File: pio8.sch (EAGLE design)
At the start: 35 parts, among them IC1 DS2408, X1 MSTBV3, X7 MSTBV5, X8 MSTBV5

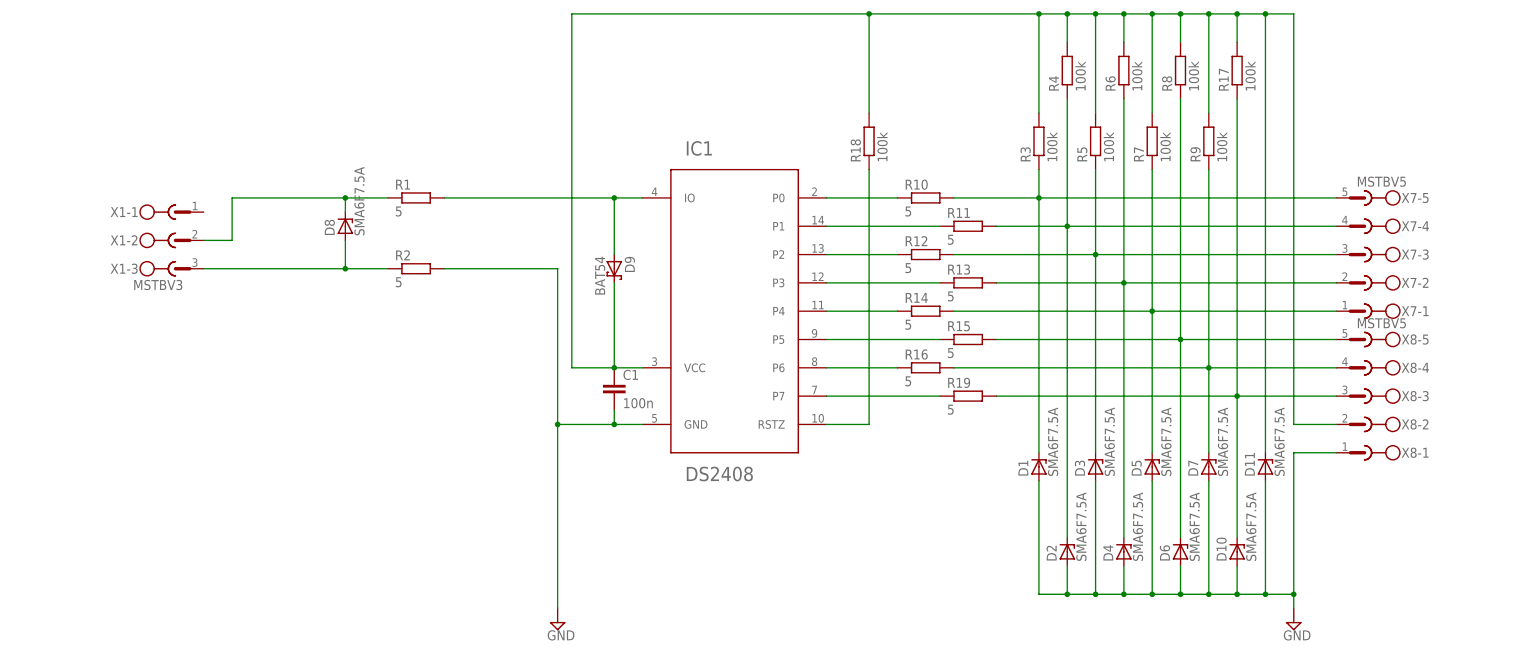
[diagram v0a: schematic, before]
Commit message: changing some values: 5 Ohm resistor to 5.1 Ohm (5 Ohm is not broadly available) selected different type of TVS diode with essentially the same ratings
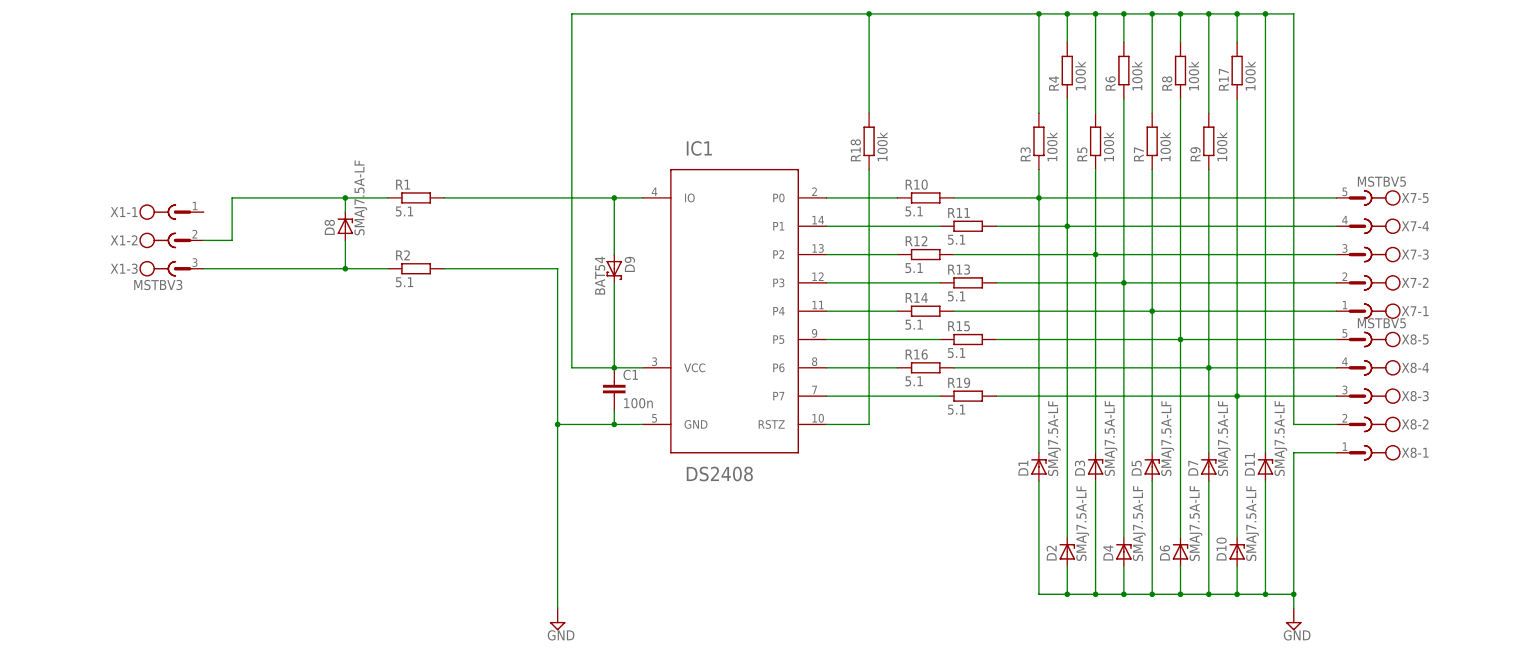
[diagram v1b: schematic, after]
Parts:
- D1, D10, D11, D2, D3, D4, D5, D6, D7, D8: value SMA6F7.5A -> SMAJ7.5A-LF
- R1, R10, R11, R12, R13, R14, R15, R16, R19, R2: value 5 -> 5.1
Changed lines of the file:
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@@
 <part name="SUPPLY1" library="supply2" deviceset="GND" device=""/>
 <part name="SUPPLY2" library="supply2" deviceset="GND" device=""/>
-<part name="R1" library="rcl" deviceset="R-EU_" device="R0402" value="5"/>
-<part name="R2" library="rcl" deviceset="R-EU_" device="R0402" value="5"/>
+<part name="R1" library="rcl" deviceset="R-EU_" device="R0402" value="5.1"/>
+<part name="R2" library="rcl" deviceset="R-EU_" device="R0402" value="5.1"/>
 <part name="D9" library="diode" deviceset="BAT54" device=""/>
 <part name="C1" library="rcl" deviceset="C-EU" device="C0402K" value="100n"/>
@@
 <part name="R8" library="resistor" deviceset="R-EU_" device="R0402" value="100k"/>
 <part name="R9" library="resistor" deviceset="R-EU_" device="R0402" value="100k"/>
-<part name="D8" library="diodes" deviceset="ZENER" device="" value="SMA6F7.5A"/>
-<part name="D1" library="diodes" deviceset="ZENER" device="" value="SMA6F7.5A"/>
-<part name="D2" library="diodes" deviceset="ZENER" device="" value="SMA6F7.5A"/>
-<part name="D3" library="diodes" deviceset="ZENER" device="" value="SMA6F7.5A"/>
-<part name="D4" library="diodes" deviceset="ZENER" device="" value="SMA6F7.5A"/>
-<part name="D5" library="diodes" deviceset="ZENER" device="" value="SMA6F7.5A"/>
-<part name="D6" library="diodes" deviceset="ZENER" device="" value="SMA6F7.5A"/>
-<part name="D7" library="diodes" deviceset="ZENER" device="" value="SMA6F7.5A"/>
-<part name="R10" library="rcl" deviceset="R-EU_" device="R0402" value="5"/>
-<part name="R11" library="rcl" deviceset="R-EU_" device="R0402" value="5"/>
-<part name="R12" library="rcl" deviceset="R-EU_" device="R0402" value="5"/>
-<part name="R13" library="rcl" deviceset="R-EU_" device="R0402" value="5"/>
-<part name="R14" library="rcl" deviceset="R-EU_" device="R0402" value="5"/>
-<part name="R15" library="rcl" deviceset="R-EU_" device="R0402" value="5"/>
-<part name="R16" library="rcl" deviceset="R-EU_" device="R0402" value="5"/>
+<part name="D8" library="diodes" deviceset="ZENER" device="" value="SMAJ7.5A-LF"/>
+<part name="D1" library="diodes" deviceset="ZENER" device="" value="SMAJ7.5A-LF"/>
+<part name="D2" library="diodes" deviceset="ZENER" device="" value="SMAJ7.5A-LF"/>
+<part name="D3" library="diodes" deviceset="ZENER" device="" value="SMAJ7.5A-LF"/>
+<part name="D4" library="diodes" deviceset="ZENER" device="" value="SMAJ7.5A-LF"/>
+<part name="D5" library="diodes" deviceset="ZENER" device="" value="SMAJ7.5A-LF"/>
+<part name="D6" library="diodes" deviceset="ZENER" device="" value="SMAJ7.5A-LF"/>
+<part name="D7" library="diodes" deviceset="ZENER" device="" value="SMAJ7.5A-LF"/>
+<part name="R10" library="rcl" deviceset="R-EU_" device="R0402" value="5.1"/>
+<part name="R11" library="rcl" deviceset="R-EU_" device="R0402" value="5.1"/>
+<part name="R12" library="rcl" deviceset="R-EU_" device="R0402" value="5.1"/>
+<part name="R13" library="rcl" deviceset="R-EU_" device="R0402" value="5.1"/>
+<part name="R14" library="rcl" deviceset="R-EU_" device="R0402" value="5.1"/>
+<part name="R15" library="rcl" deviceset="R-EU_" device="R0402" value="5.1"/>
+<part name="R16" library="rcl" deviceset="R-EU_" device="R0402" value="5.1"/>
 <part name="R18" library="resistor" deviceset="R-EU_" device="R0402" value="100k"/>
 <part name="X7" library="con-phoenix-508" deviceset="MSTBV5" device=""/>
 <part name="X8" library="con-phoenix-508" deviceset="MSTBV5" device=""/>
 <part name="R17" library="resistor" deviceset="R-EU_" device="R0402" value="100k"/>
-<part name="D10" library="diodes" deviceset="ZENER" device="" value="SMA6F7.5A"/>
-<part name="D11" library="diodes" deviceset="ZENER" device="" value="SMA6F7.5A"/>
-<part name="R19" library="rcl" deviceset="R-EU_" device="R0402" value="5"/>
+<part name="D10" library="diodes" deviceset="ZENER" device="" value="SMAJ7.5A-LF"/>
+<part name="D11" library="diodes" deviceset="ZENER" device="" value="SMAJ7.5A-LF"/>
+<part name="R19" library="rcl" deviceset="R-EU_" device="R0402" value="5.1"/>
 <part name="X1" library="con-phoenix-508" deviceset="MSTBV3" device=""/>
 </parts>

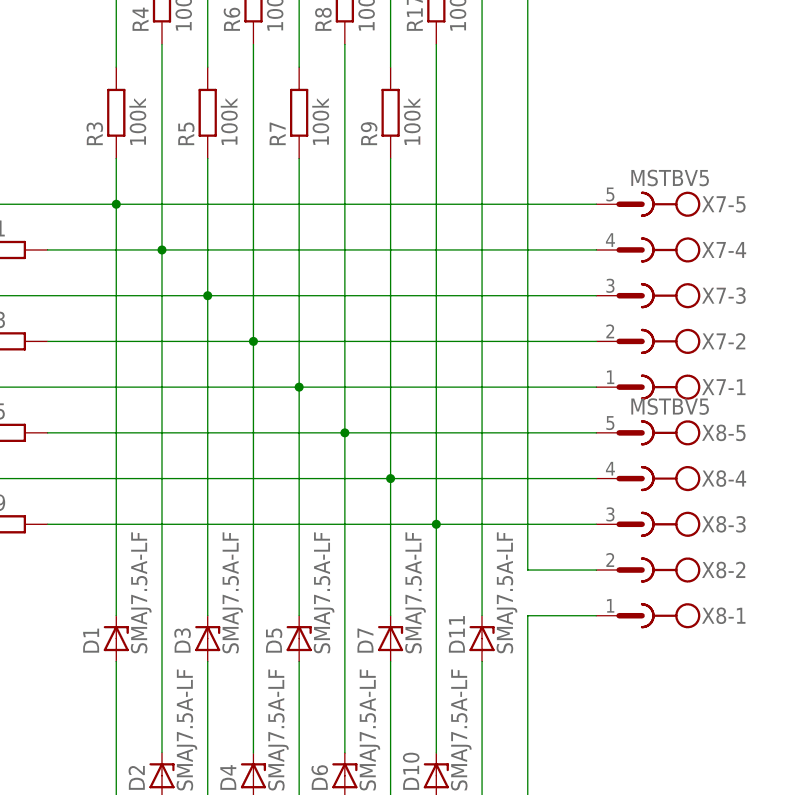
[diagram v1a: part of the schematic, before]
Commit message: rotating connectors to resolve issue #1 while maintaining IO and GND/VCC pinout but rotating pinout for the one wire connector (to keep the pin numbering the same as other 1-wire devices have)
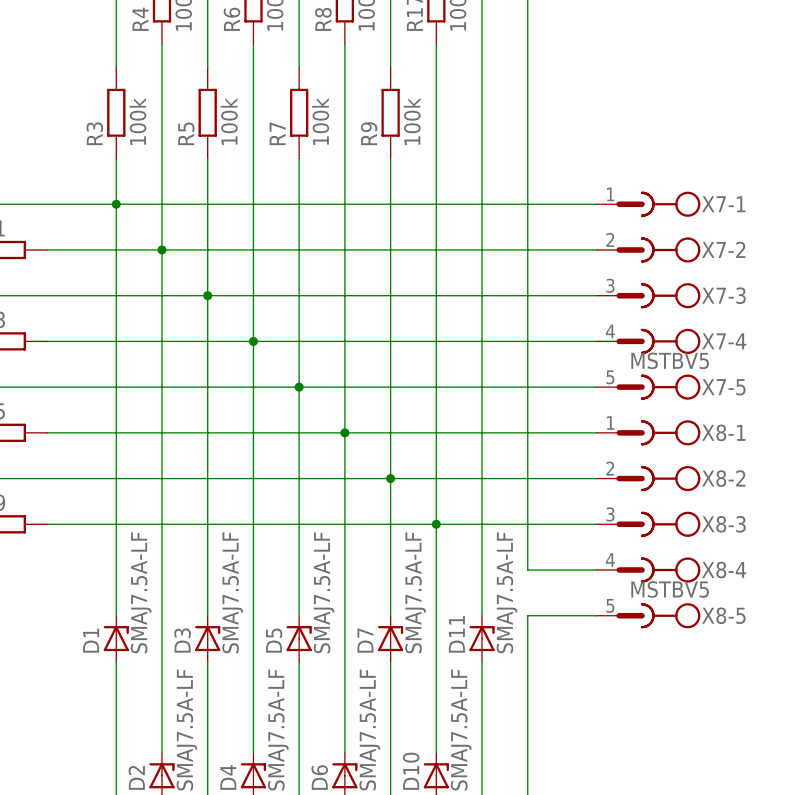
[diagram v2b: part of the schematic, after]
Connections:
- net GND: now also X8-5.1; no longer X8-1.1
- net N$1: now also X7-1.1; no longer X7-5.1
- net N$11: now also X8-4.1; no longer X8-2.1
- net N$2: now also X7-2.1; no longer X7-4.1
- net N$4: now also X7-4.1; no longer X7-2.1
- net N$5: now also X7-5.1; no longer X7-1.1
- net N$6: now also X8-1.1; no longer X8-5.1
- net N$7: now also X8-2.1; no longer X8-4.1
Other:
- moved on the sheet: X7-1, X7-2, X7-4, X7-5, X8-1, X8-2, X8-4, X8-5
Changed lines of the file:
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@@
 <instance part="R16" gate="G$1" x="134.62" y="48.26"/>
 <instance part="R18" gate="G$1" x="124.46" y="88.9" rot="R90"/>
-<instance part="X7" gate="-1" x="213.36" y="58.42" rot="R180"/>
-<instance part="X7" gate="-2" x="213.36" y="63.5" rot="R180"/>
+<instance part="X7" gate="-1" x="213.36" y="78.74" rot="R180"/>
+<instance part="X7" gate="-2" x="213.36" y="73.66" rot="R180"/>
 <instance part="X7" gate="-3" x="213.36" y="68.58" rot="R180"/>
-<instance part="X7" gate="-4" x="213.36" y="73.66" rot="R180"/>
-<instance part="X7" gate="-5" x="213.36" y="78.74" rot="R180"/>
-<instance part="X8" gate="-1" x="213.36" y="33.02" rot="R180"/>
-<instance part="X8" gate="-2" x="213.36" y="38.1" rot="R180"/>
+<instance part="X7" gate="-4" x="213.36" y="63.5" rot="R180"/>
+<instance part="X7" gate="-5" x="213.36" y="58.42" rot="R180"/>
+<instance part="X8" gate="-1" x="213.36" y="53.34" rot="R180"/>
+<instance part="X8" gate="-2" x="213.36" y="48.26" rot="R180"/>
 <instance part="X8" gate="-3" x="213.36" y="43.18" rot="R180"/>
-<instance part="X8" gate="-4" x="213.36" y="48.26" rot="R180"/>
-<instance part="X8" gate="-5" x="213.36" y="53.34" rot="R180"/>
+<instance part="X8" gate="-4" x="213.36" y="38.1" rot="R180"/>
+<instance part="X8" gate="-5" x="213.36" y="33.02" rot="R180"/>
 <instance part="R17" gate="G$1" x="190.5" y="101.6" rot="R90"/>
 <instance part="D10" gate="G$1" x="190.5" y="15.24" rot="R90"/>
@@
 <pinref part="R10" gate="G$1" pin="2"/>
 <wire x1="139.7" y1="78.74" x2="154.94" y2="78.74" width="0.1524" layer="91"/>
-<pinref part="X7" gate="-5" pin="1"/>
+<pinref part="X7" gate="-1" pin="1"/>
 <wire x1="154.94" y1="78.74" x2="208.28" y2="78.74" width="0.1524" layer="91"/>
 </segment>
@@
 <pinref part="R11" gate="G$1" pin="2"/>
 <wire x1="147.32" y1="73.66" x2="160.02" y2="73.66" width="0.1524" layer="91"/>
-<pinref part="X7" gate="-4" pin="1"/>
-<wire x1="160.02" y1="73.66" x2="208.28" y2="73.66" width="0.1524" layer="91"/>
+<pinref part="X7" gate="-2" pin="1"/>
+<wire x1="208.28" y1="73.66" x2="160.02" y2="73.66" width="0.1524" layer="91"/>
 </segment>
 </net>
@@
 <pinref part="R13" gate="G$1" pin="2"/>
 <wire x1="147.32" y1="63.5" x2="170.18" y2="63.5" width="0.1524" layer="91"/>
-<pinref part="X7" gate="-2" pin="1"/>
-<wire x1="170.18" y1="63.5" x2="208.28" y2="63.5" width="0.1524" layer="91"/>
+<pinref part="X7" gate="-4" pin="1"/>
+<wire x1="208.28" y1="63.5" x2="170.18" y2="63.5" width="0.1524" layer="91"/>
 </segment>
 </net>
@@
 <pinref part="R14" gate="G$1" pin="2"/>
 <wire x1="139.7" y1="58.42" x2="175.26" y2="58.42" width="0.1524" layer="91"/>
-<pinref part="X7" gate="-1" pin="1"/>
+<pinref part="X7" gate="-5" pin="1"/>
 <wire x1="175.26" y1="58.42" x2="208.28" y2="58.42" width="0.1524" layer="91"/>
 </segment>
@@
 <pinref part="R15" gate="G$1" pin="2"/>
 <wire x1="147.32" y1="53.34" x2="180.34" y2="53.34" width="0.1524" layer="91"/>
-<pinref part="X8" gate="-5" pin="1"/>
-<wire x1="180.34" y1="53.34" x2="208.28" y2="53.34" width="0.1524" layer="91"/>
+<pinref part="X8" gate="-1" pin="1"/>
+<wire x1="208.28" y1="53.34" x2="180.34" y2="53.34" width="0.1524" layer="91"/>
 </segment>
 </net>
@@
 <pinref part="R16" gate="G$1" pin="2"/>
 <wire x1="139.7" y1="48.26" x2="185.42" y2="48.26" width="0.1524" layer="91"/>
-<pinref part="X8" gate="-4" pin="1"/>
-<wire x1="208.28" y1="48.26" x2="185.42" y2="48.26" width="0.1524" layer="91"/>
+<pinref part="X8" gate="-2" pin="1"/>
+<wire x1="185.42" y1="48.26" x2="208.28" y2="48.26" width="0.1524" layer="91"/>
 </segment>
 </net>
@@
 <wire x1="195.58" y1="27.94" x2="195.58" y2="7.62" width="0.1524" layer="91"/>
 <junction x="195.58" y="7.62"/>
-<pinref part="X8" gate="-1" pin="1"/>
+<pinref part="X8" gate="-5" pin="1"/>
 <wire x1="208.28" y1="33.02" x2="200.66" y2="33.02" width="0.1524" layer="91"/>
 </segment>
@@
 <junction x="195.58" y="111.76"/>
 <wire x1="200.66" y1="111.76" x2="200.66" y2="38.1" width="0.1524" layer="91"/>
-<pinref part="X8" gate="-2" pin="1"/>
-<wire x1="208.28" y1="38.1" x2="200.66" y2="38.1" width="0.1524" layer="91"/>
+<pinref part="X8" gate="-4" pin="1"/>
+<wire x1="200.66" y1="38.1" x2="208.28" y2="38.1" width="0.1524" layer="91"/>
 </segment>
 </net>
@@
 <wire x1="147.32" y1="43.18" x2="190.5" y2="43.18" width="0.1524" layer="91"/>
 <pinref part="X8" gate="-3" pin="1"/>
-<wire x1="190.5" y1="43.18" x2="208.28" y2="43.18" width="0.1524" layer="91"/>
-</segment>
-</net>
+<wire x1="208.28" y1="43.18" x2="190.5" y2="43.18" width="0.1524" layer="91"/>
+</segment>
+</net>
